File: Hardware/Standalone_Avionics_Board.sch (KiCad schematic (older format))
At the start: 4 parts

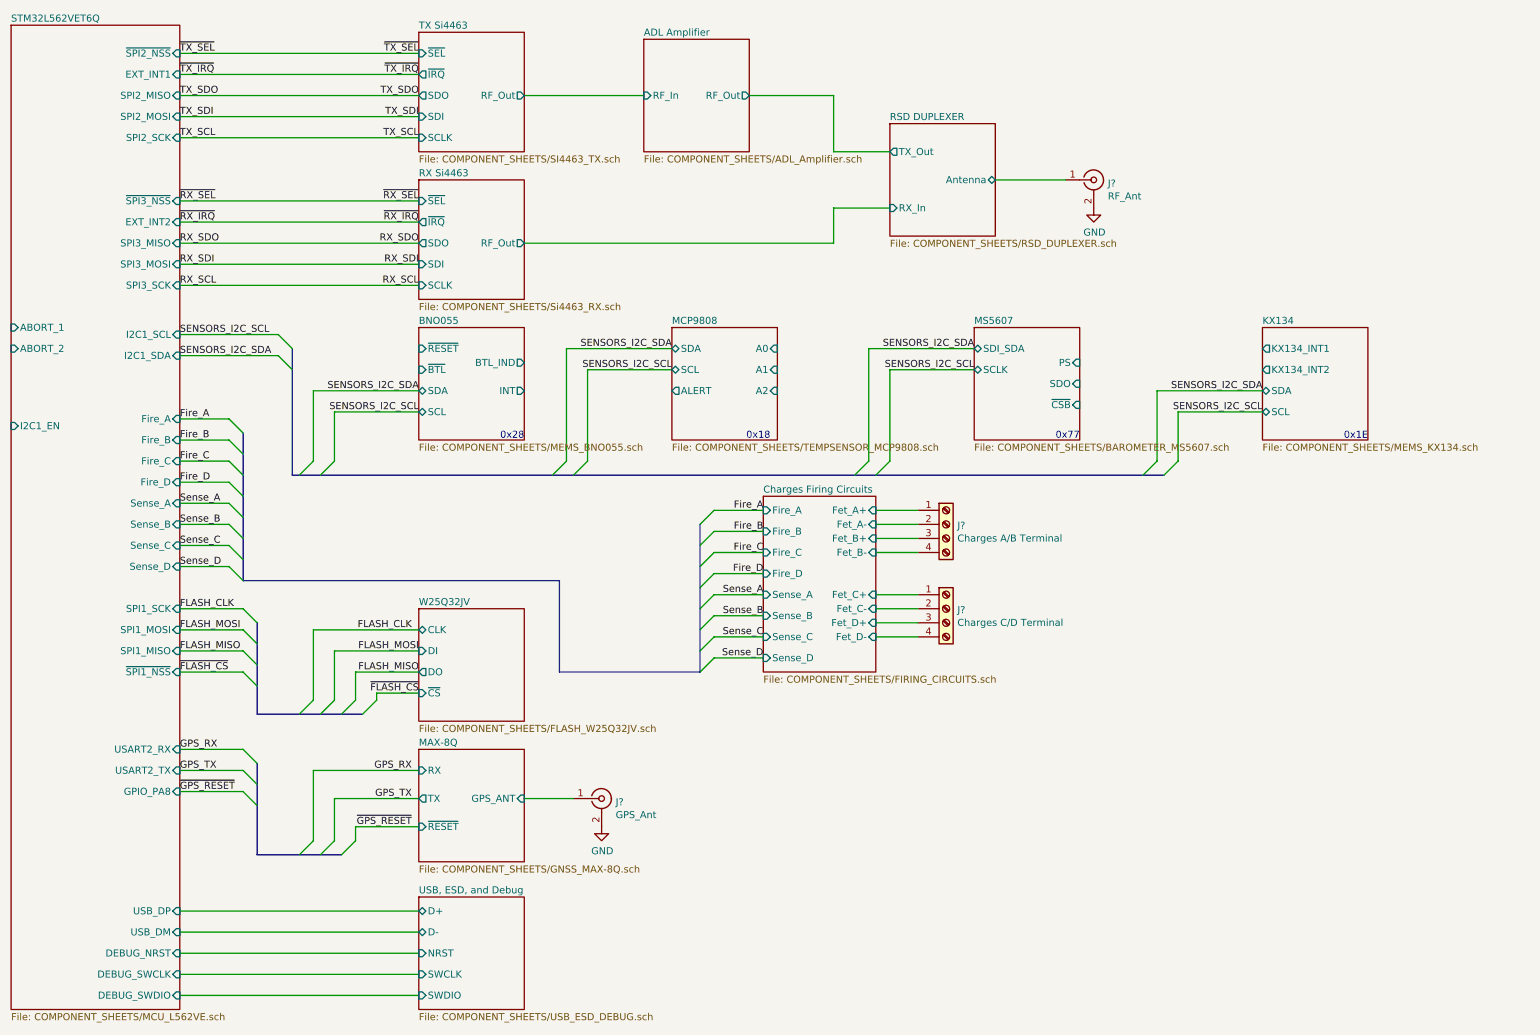
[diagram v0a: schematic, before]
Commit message: Annotated and Assigned Footprints
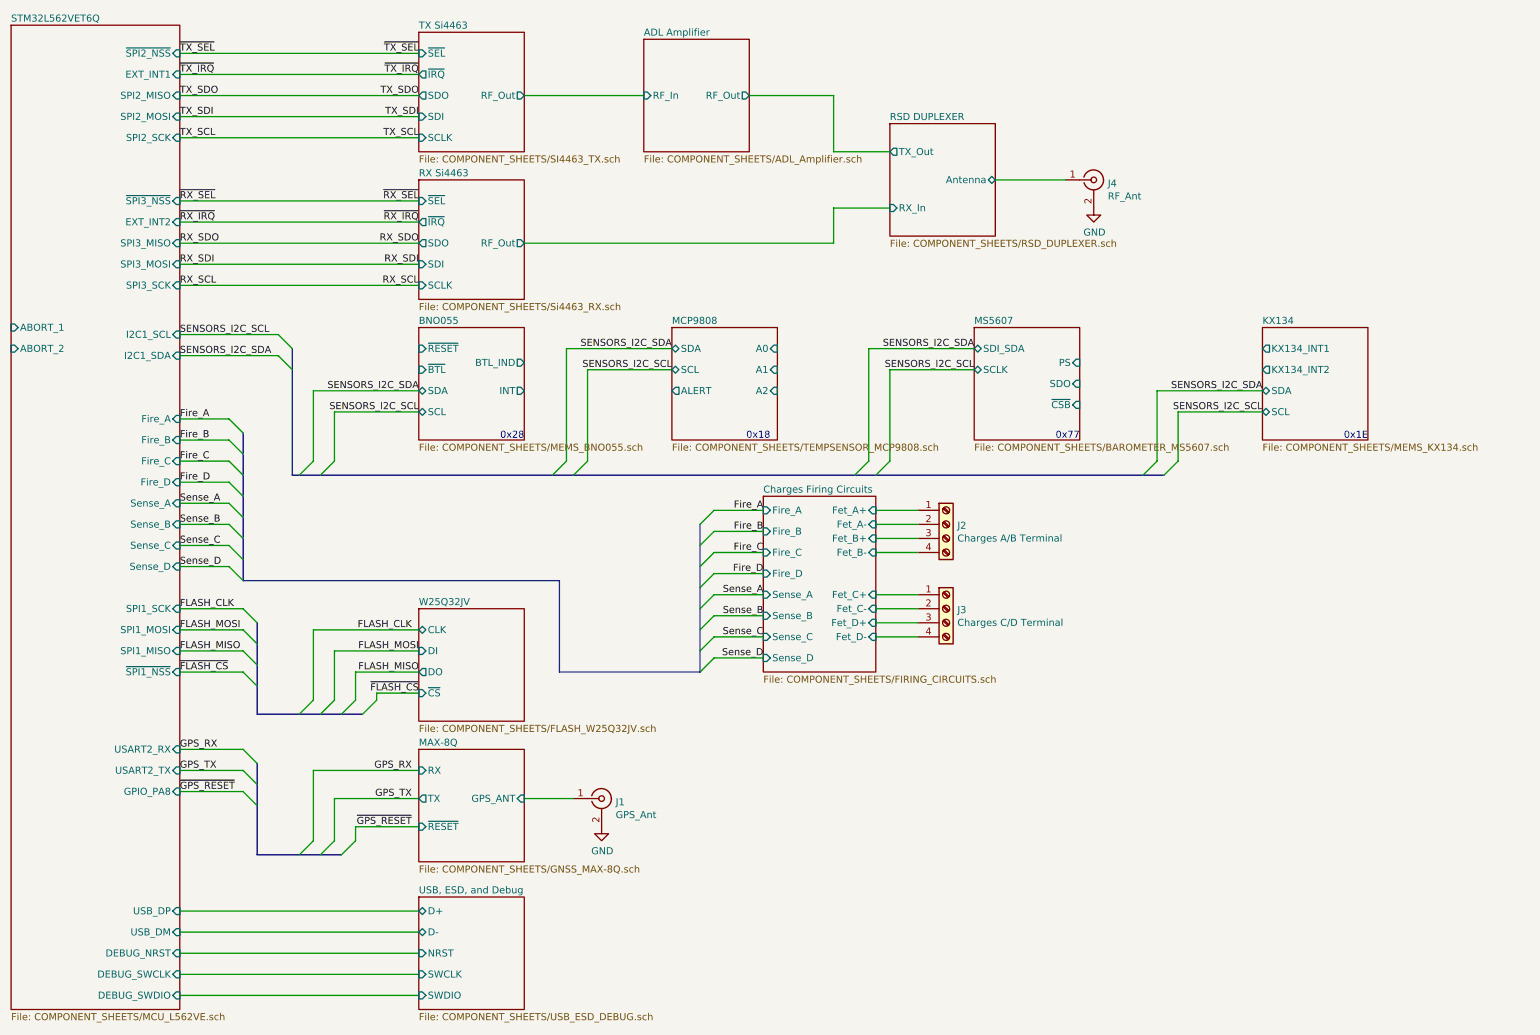
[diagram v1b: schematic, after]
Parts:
- J1, J4: renamed from J?; footprint (none) -> Connector_Coaxial:SMA_Amphenol_132134-11_Vertical
- J2, J3: renamed from J?; footprint (none) -> TerminalBlock_Phoenix:TerminalBlock_Phoenix_MKDS-1,5-4_1x04_P5.00mm_Horizontal
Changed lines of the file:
@@
 $EndDescr
 $Comp
-L Connector:Conn_Coaxial J?
+L Connector:Conn_Coaxial J1
 U 1 1 61B49554
 P 4800 6100
-F 0 "J?" H 4900 6075 50  0000 L CNN
+F 0 "J1" H 4900 6075 50  0000 L CNN
 F 1 "GPS_Ant" H 4900 5984 50  0000 L CNN
-F 2 "" H 4800 6100 50  0001 C CNN
+F 2 "Connector_Coaxial:SMA_Amphenol_132134-11_Vertical" H 4800 6100 50  0001 C CNN
 F 3 " ~" H 4800 6100 50  0001 C CNN
 	1    4800 6100
@@
 $EndComp
 $Comp
-L power:GND #PWR?
+L power:GND #PWR01
 U 1 1 61B49D74
 P 4800 6300
-F 0 "#PWR?" H 4800 6050 50  0001 C CNN
+F 0 "#PWR01" H 4800 6050 50  0001 C CNN
 F 1 "GND" H 4805 6127 50  0000 C CNN
 F 2 "" H 4800 6300 50  0001 C CNN
@@
 	4250 6100 4600 6100
 $Comp
-L power:GND #PWR?
+L power:GND #PWR02
 U 1 1 61B49CC6
 P 8300 1900
-F 0 "#PWR?" H 8300 1650 50  0001 C CNN
+F 0 "#PWR02" H 8300 1650 50  0001 C CNN
 F 1 "GND" H 8305 1727 50  0000 C CNN
 F 2 "" H 8300 1900 50  0001 C CNN
@@
 $EndComp
 $Comp
-L Connector:Conn_Coaxial J?
+L Connector:Conn_Coaxial J4
 U 1 1 61B4987D
 P 8300 1700
-F 0 "J?" H 8400 1675 50  0000 L CNN
+F 0 "J4" H 8400 1675 50  0000 L CNN
 F 1 "RF_Ant" H 8400 1584 50  0000 L CNN
-F 2 "" H 8300 1700 50  0001 C CNN
+F 2 "Connector_Coaxial:SMA_Amphenol_132134-11_Vertical" H 8300 1700 50  0001 C CNN
 F 3 " ~" H 8300 1700 50  0001 C CNN
 	1    8300 1700
@@
 P 7250 4150
 AR Path="/61C104EE/61DE5119" Ref="J?"  Part="1"
-AR Path="/61DE5119" Ref="J?"  Part="1"
-F 0 "J?" H 7330 4142 50  0000 L CNN
+AR Path="/61DE5119" Ref="J2"  Part="1"
+F 0 "J2" H 7330 4142 50  0000 L CNN
 F 1 "Charges A/B Terminal" H 7330 4051 50  0000 L CNN
-F 2 "" H 7250 4150 50  0001 C CNN
+F 2 "TerminalBlock_Phoenix:TerminalBlock_Phoenix_MKDS-1,5-4_1x04_P5.00mm_Horizontal" H 7250 4150 50  0001 C CNN
 F 3 "~" H 7250 4150 50  0001 C CNN
 	1    7250 4150
@@
 P 7250 4750
 AR Path="/61C104EE/61DE7D04" Ref="J?"  Part="1"
-AR Path="/61DE7D04" Ref="J?"  Part="1"
-F 0 "J?" H 7330 4742 50  0000 L CNN
+AR Path="/61DE7D04" Ref="J3"  Part="1"
+F 0 "J3" H 7330 4742 50  0000 L CNN
 F 1 "Charges C/D Terminal" H 7330 4651 50  0000 L CNN
-F 2 "" H 7250 4750 50  0001 C CNN
+F 2 "TerminalBlock_Phoenix:TerminalBlock_Phoenix_MKDS-1,5-4_1x04_P5.00mm_Horizontal" H 7250 4750 50  0001 C CNN
 F 3 "~" H 7250 4750 50  0001 C CNN
 	1    7250 4750
@@
 F26 "GPIO_PA8" I R 1800 6050 50
 F27 "DEBUG_NRST" I R 1800 7200 50
-F28 "I2C1_EN" I L 600 3450 50
-F29 "Fire_A" I R 1800 3400 50
-F30 "Fire_B" I R 1800 3550 50
-F31 "Fire_C" I R 1800 3700 50
-F32 "Fire_D" I R 1800 3850 50
-F33 "Sense_A" I R 1800 4000 50
-F34 "Sense_B" I R 1800 4150 50
-F35 "Sense_C" I R 1800 4300 50
-F36 "Sense_D" I R 1800 4450 50
+F28 "Fire_A" I R 1800 3400 50
+F29 "Fire_B" I R 1800 3550 50
+F30 "Fire_C" I R 1800 3700 50
+F31 "Fire_D" I R 1800 3850 50
+F32 "Sense_A" I R 1800 4000 50
+F33 "Sense_B" I R 1800 4150 50
+F34 "Sense_C" I R 1800 4300 50
+F35 "Sense_D" I R 1800 4450 50
 $EndSheet
 Wire Bus Line

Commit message: Replaced 2x 4pole terminal blocks with 1x 8pole
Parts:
- removed J2: Charges A/B Terminal, TerminalBlock_Phoenix:TerminalBlock_Phoenix_MKDS-1,5-4_1x04_P5.00mm_Horizontal, symbol Connector:Screw_Terminal_01x04
- removed J3: Charges C/D Terminal, TerminalBlock_Phoenix:TerminalBlock_Phoenix_MKDS-1,5-4_1x04_P5.00mm_Horizontal, symbol Connector:Screw_Terminal_01x04
- added J2: Charges Terminal Block, TerminalBlock_Phoenix:TerminalBlock_Phoenix_MKDS-1,5-8-5.08_1x08_P5.08mm_Horizontal, symbol Connector:Screw_Terminal_01x08
- renumbered J4 to J3
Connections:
- net Charges Firing Circuits/Fet_A+: now also J2.1 (Pin_1)
- net Charges Firing Circuits/Fet_A-: now also J2.2 (Pin_2)
- net Charges Firing Circuits/Fet_B+: now also J2.3 (Pin_3)
- net Charges Firing Circuits/Fet_B-: now also J2.4 (Pin_4)
- net Charges Firing Circuits/Fet_C+: now also J2.5 (Pin_5)
- net Charges Firing Circuits/Fet_C-: now also J2.6 (Pin_6)
- net Charges Firing Circuits/Fet_D+: now also J2.7 (Pin_7)
- net Charges Firing Circuits/Fet_D-: now also J2.8 (Pin_8)
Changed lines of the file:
@@
 $EndComp
 $Comp
-L Connector:Conn_Coaxial J4
+L Connector:Conn_Coaxial J3
 U 1 1 61B4987D
 P 8300 1700
-F 0 "J4" H 8400 1675 50  0000 L CNN
+F 0 "J3" H 8400 1675 50  0000 L CNN
 F 1 "RF_Ant" H 8400 1584 50  0000 L CNN
 F 2 "Connector_Coaxial:SMA_Amphenol_132134-11_Vertical" H 8300 1700 50  0001 C CNN
@@
 F6 "SWDIO" I L 3500 7500 50
 $EndSheet
-$Comp
-L Connector:Screw_Terminal_01x04 J?
-U 1 1 61DE5119
-P 7250 4150
-AR Path="/61C104EE/61DE5119" Ref="J?"  Part="1"
-AR Path="/61DE5119" Ref="J2"  Part="1"
-F 0 "J2" H 7330 4142 50  0000 L CNN
-F 1 "Charges A/B Terminal" H 7330 4051 50  0000 L CNN
-F 2 "TerminalBlock_Phoenix:TerminalBlock_Phoenix_MKDS-1,5-4_1x04_P5.00mm_Horizontal" H 7250 4150 50  0001 C CNN
-F 3 "~" H 7250 4150 50  0001 C CNN
-	1    7250 4150
-	1    0    0    -1
-$EndComp
-$Comp
-L Connector:Screw_Terminal_01x04 J?
-U 1 1 61DE7D04
-P 7250 4750
-AR Path="/61C104EE/61DE7D04" Ref="J?"  Part="1"
-AR Path="/61DE7D04" Ref="J3"  Part="1"
-F 0 "J3" H 7330 4742 50  0000 L CNN
-F 1 "Charges C/D Terminal" H 7330 4651 50  0000 L CNN
-F 2 "TerminalBlock_Phoenix:TerminalBlock_Phoenix_MKDS-1,5-4_1x04_P5.00mm_Horizontal" H 7250 4750 50  0001 C CNN
-F 3 "~" H 7250 4750 50  0001 C CNN
-	1    7250 4750
-	1    0    0    -1
-$EndComp
 Entry Wire Line
 	2150 4450 2250 4550
@@
 Wire Bus Line
 	4500 4550 2250 4550
-$Sheet
-S 5950 3950 800  1250
-U 61C104EE
-F0 "Charges Firing Circuits" 50
-F1 "COMPONENT_SHEETS/FIRING_CIRCUITS.sch" 50
-F2 "Fire_A" I L 5950 4050 50
-F3 "Fire_B" I L 5950 4200 50
-F4 "Fire_C" I L 5950 4350 50
-F5 "Fire_D" I L 5950 4500 50
-F6 "Sense_A" I L 5950 4650 50
-F7 "Sense_B" I L 5950 4800 50
-F8 "Sense_C" I L 5950 4950 50
-F9 "Sense_D" I L 5950 5100 50
-F10 "Fet_A+" I R 6750 4050 50
-F11 "Fet_B+" I R 6750 4250 50
-F12 "Fet_C+" I R 6750 4650 50
-F13 "Fet_D+" I R 6750 4850 50
-F14 "Fet_A-" I R 6750 4150 50
-F15 "Fet_B-" I R 6750 4350 50
-F16 "Fet_C-" I R 6750 4750 50
-F17 "Fet_D-" I R 6750 4950 50
-$EndSheet
-Wire Wire Line
-	6750 4050 7050 4050
-Wire Wire Line
-	6750 4950 7050 4950
-Wire Wire Line
-	7050 4850 6750 4850
-Wire Wire Line
-	6750 4750 7050 4750
-Wire Wire Line
-	7050 4650 6750 4650
-Wire Wire Line
-	6750 4350 7050 4350
-Wire Wire Line
-	7050 4250 6750 4250
-Wire Wire Line
-	6750 4150 7050 4150
 $Sheet
 S 600  600  1200 7000
@@
 F5 "~CS" I L 3500 5350 50
 $EndSheet
+$Comp
+L Connector:Screw_Terminal_01x08 J2
+U 1 1 61EBDC84
+P 7450 4450
+F 0 "J2" H 7530 4442 50  0000 L CNN
+F 1 "Charges Terminal Block" H 7530 4351 50  0000 L CNN
+F 2 "TerminalBlock_Phoenix:TerminalBlock_Phoenix_MKDS-1,5-8-5.08_1x08_P5.08mm_Horizontal" H 7450 4450 50  0001 C CNN
+F 3 "~" H 7450 4450 50  0001 C CNN
+	1    7450 4450
+	1    0    0    -1
+$EndComp
+$Sheet
+S 5950 3950 800  1250
+U 61C104EE
+F0 "Charges Firing Circuits" 50
+F1 "COMPONENT_SHEETS/FIRING_CIRCUITS.sch" 50
+F2 "Fire_A" I L 5950 4050 50
+F3 "Fire_B" I L 5950 4200 50
+F4 "Fire_C" I L 5950 4350 50
+F5 "Fire_D" I L 5950 4500 50
+F6 "Sense_A" I L 5950 4650 50
+F7 "Sense_B" I L 5950 4800 50
+F8 "Sense_C" I L 5950 4950 50
+F9 "Sense_D" I L 5950 5100 50
+F10 "Fet_A+" I R 6750 4150 50
+F11 "Fet_B+" I R 6750 4350 50
+F12 "Fet_C+" I R 6750 4550 50
+F13 "Fet_D+" I R 6750 4750 50
+F14 "Fet_A-" I R 6750 4250 50
+F15 "Fet_B-" I R 6750 4450 50
+F16 "Fet_C-" I R 6750 4650 50
+F17 "Fet_D-" I R 6750 4850 50
+$EndSheet
+Wire Wire Line
+	6750 4150 7250 4150
+Wire Wire Line
+	7250 4250 6750 4250
+Wire Wire Line
+	6750 4350 7250 4350
+Wire Wire Line
+	7250 4450 6750 4450
+Wire Wire Line
+	6750 4550 7250 4550
+Wire Wire Line
+	7250 4650 6750 4650
+Wire Wire Line
+	6750 4750 7250 4750
+Wire Wire Line
+	7250 4850 6750 4850
 Wire Bus Line
 	2600 2900 2600 3800

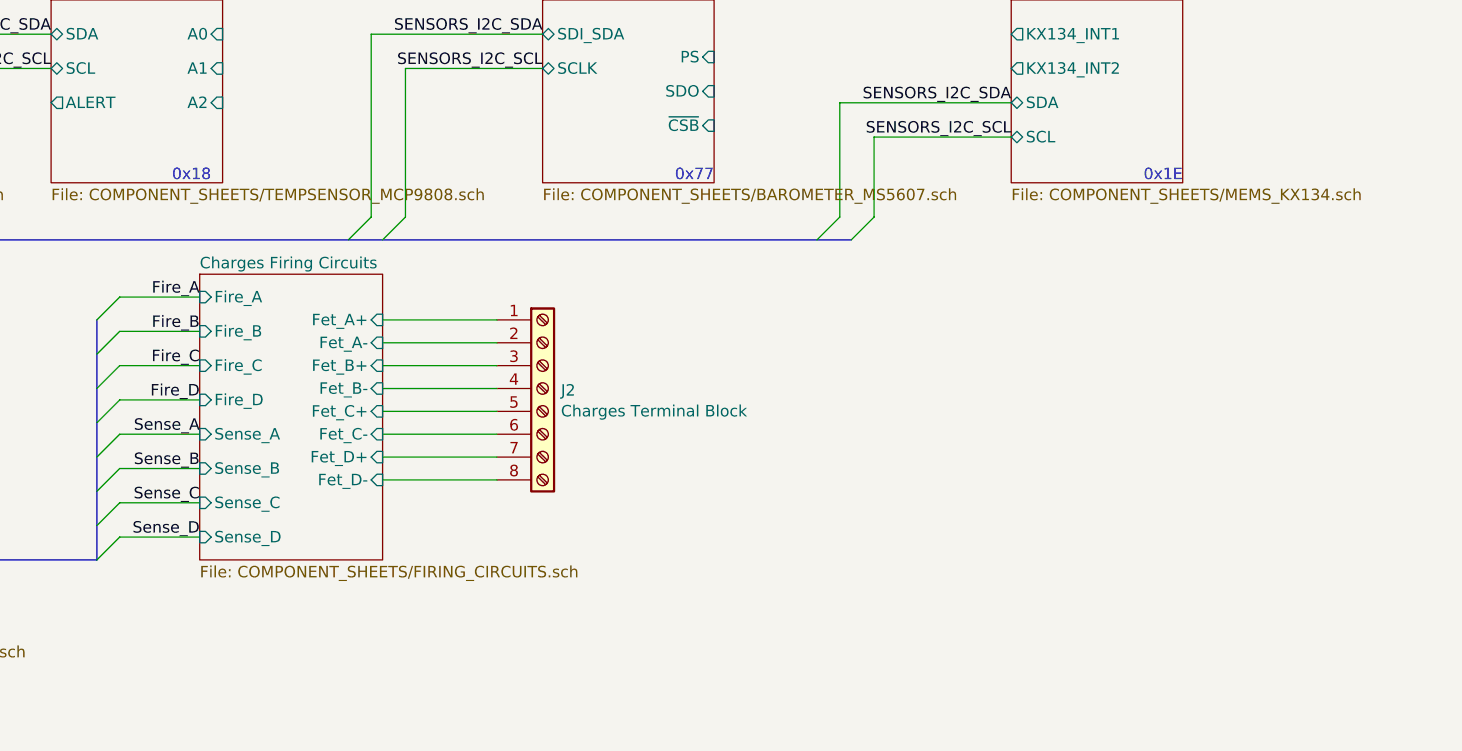
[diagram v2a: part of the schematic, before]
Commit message: Added status LEDs to MCU
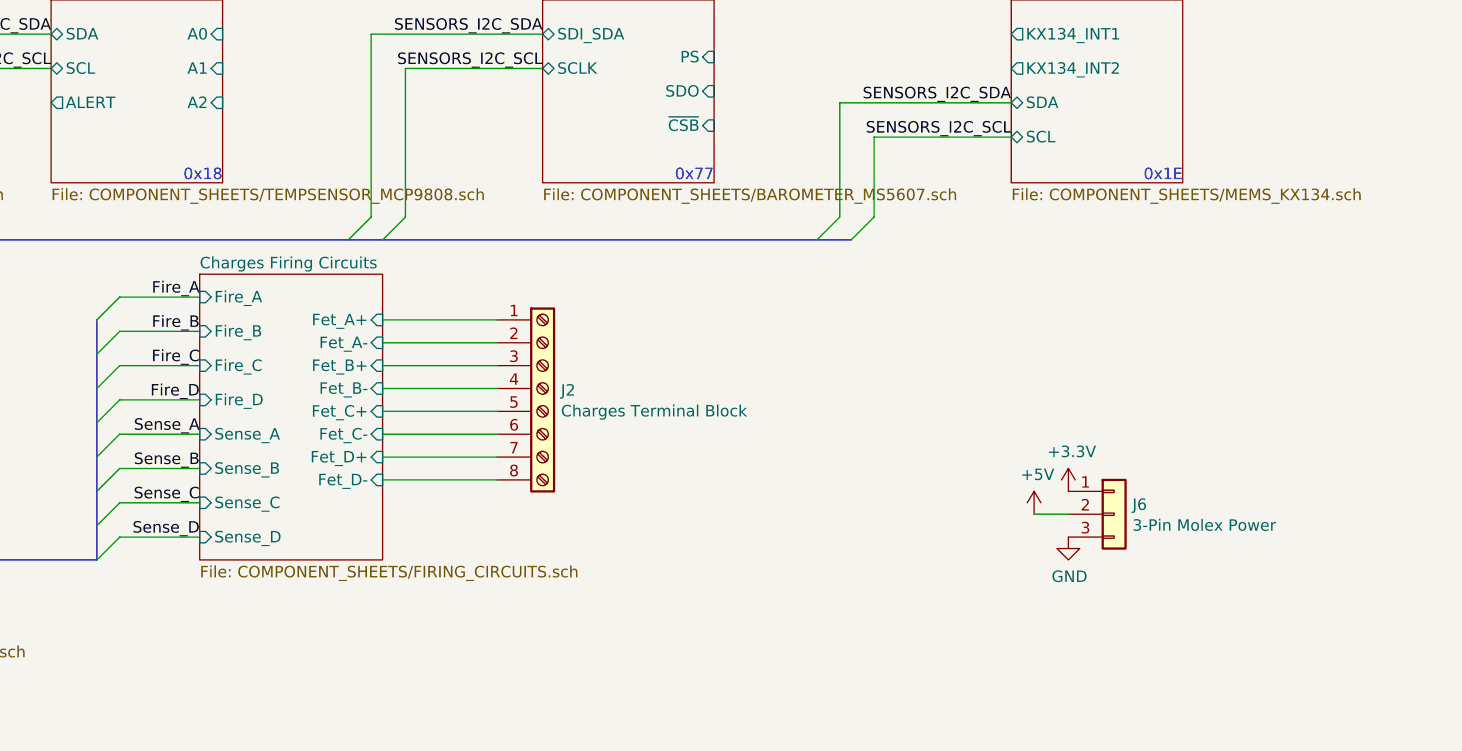
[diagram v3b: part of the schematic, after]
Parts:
- added J6: 3-Pin Molex Power, Connector_Molex:Molex_KK-254_AE-6410-03A_1x03_P2.54mm_Vertical, symbol Connector_Generic:Conn_01x03
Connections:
- net GND: now also J6.3 (Pin_3)
- new net +3V3: J6.1 (Pin_1)
- new net +5V: J6.2 (Pin_2)
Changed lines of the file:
@@
 Text Notes 8200 3550 2    50   ~ 0
 0x77
-Text Notes 6000 3550 2    50   ~ 0
+Text Notes 6050 3550 2    50   ~ 0
 0x18
 Text Notes 4250 3550 2    50   ~ 0
@@
 Wire Wire Line
 	7250 4850 6750 4850
+$Comp
+L power:+3.3V #PWR086
+U 1 1 61B21EEA
+P 9750 4900
+F 0 "#PWR086" H 9750 4750 50  0001 C CNN
+F 1 "+3.3V" H 9765 5073 50  0000 C CNN
+F 2 "" H 9750 4900 50  0001 C CNN
+F 3 "" H 9750 4900 50  0001 C CNN
+	1    9750 4900
+	1    0    0    -1
+$EndComp
+$Comp
+L power:GND #PWR087
+U 1 1 61B228F3
+P 9750 5100
+F 0 "#PWR087" H 9750 4850 50  0001 C CNN
+F 1 "GND" H 9755 4927 50  0000 C CNN
+F 2 "" H 9750 5100 50  0001 C CNN
+F 3 "" H 9750 5100 50  0001 C CNN
+	1    9750 5100
+	1    0    0    -1
+$EndComp
+$Comp
+L Connector_Generic:Conn_01x03 J6
+U 1 1 61B22E7C
+P 9950 5000
+F 0 "J6" H 10030 5042 50  0000 L CNN
+F 1 "3-Pin Molex Power" H 10030 4951 50  0000 L CNN
+F 2 "Connector_Molex:Molex_KK-254_AE-6410-03A_1x03_P2.54mm_Vertical" H 9950 5000 50  0001 C CNN
+F 3 "~" H 9950 5000 50  0001 C CNN
+	1    9950 5000
+	1    0    0    -1
+$EndComp
+$Comp
+L power:+5V #PWR085
+U 1 1 61B248E6
+P 9600 5000
+F 0 "#PWR085" H 9600 4850 50  0001 C CNN
+F 1 "+5V" H 9615 5173 50  0000 C CNN
+F 2 "" H 9600 5000 50  0001 C CNN
+F 3 "" H 9600 5000 50  0001 C CNN
+	1    9600 5000
+	1    0    0    -1
+$EndComp
+Wire Wire Line
+	9750 5000 9600 5000
 Wire Bus Line
 	2600 2900 2600 3800
